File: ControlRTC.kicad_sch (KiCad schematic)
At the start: 29 parts, among them M1 Fan_4pin, SW1 SW_POWER, SW2 SW_RESET, SW3 SW_USER, SW5 SW_RECOVERY, U16 74LVC07APW, U17 LP5569RTWR, U18 PCF85063AT, Y2 X32K768S301

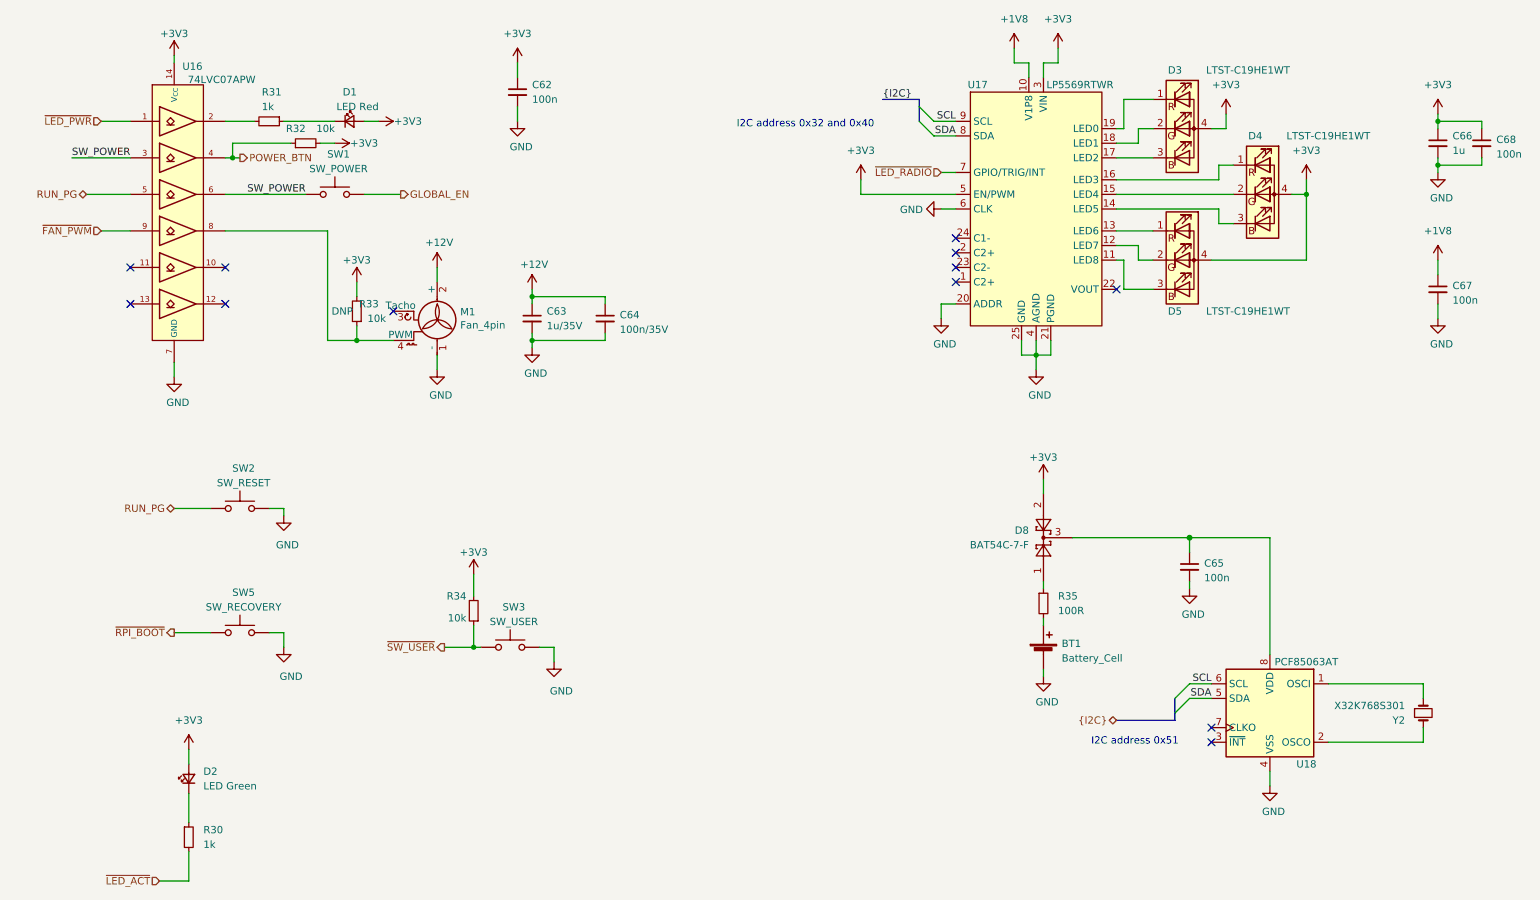
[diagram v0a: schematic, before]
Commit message: Redesign buttons/switches
Remove power/reset/recovery switch. Power and reset is not really required
and recovery mode (USB Boot) can be triggered via jumper. Make the Fan
and RPiLED a new separate config so we can leave them unpopulated. Add a
second GPIO controlled switch.

Fixes: #16

Signed-off-by: Stefan Agner <stefan@agner.ch>
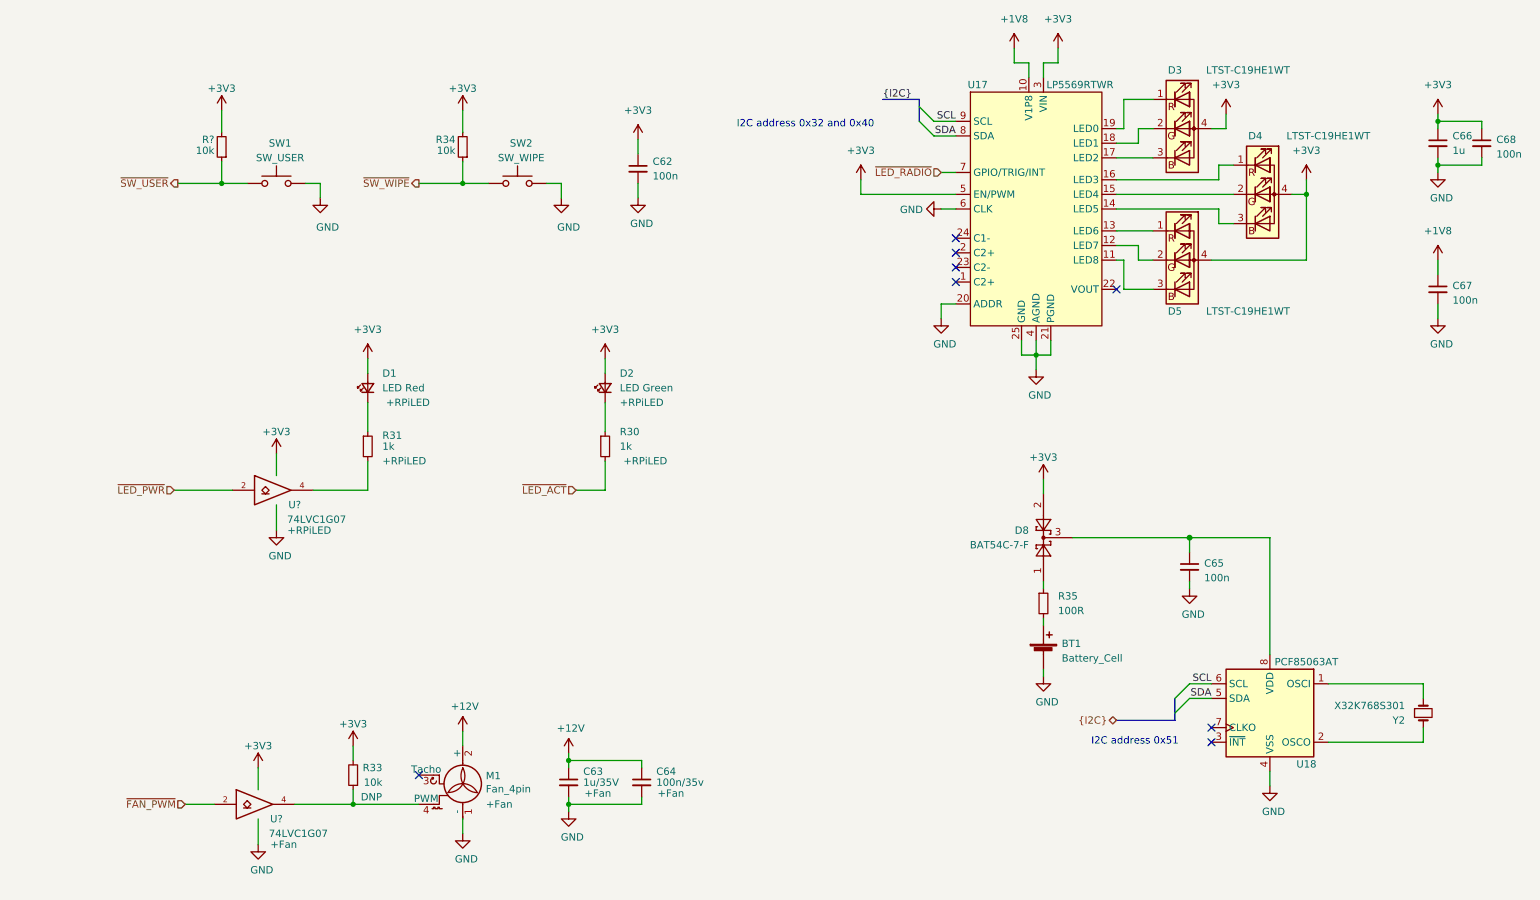
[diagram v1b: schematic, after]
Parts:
- removed R32: 10k, Resistor_SMD:R_0402_1005Metric, symbol Device:R_Small
- removed SW2: SW_RESET, Button_Switch_THT:SW_Tactile_SPST_Angled_PTS645Vx39-2LFS, symbol Switch:SW_Push
- removed SW5: SW_RECOVERY, Button_Switch_SMD:SW_SPST_B3U-3100P-B, symbol Switch:SW_Push
- removed U16: 74LVC07APW, Package_SO:TSSOP-14_4.4x5mm_P0.65mm, symbol LightBlue:74LVC07A
- added R?: 10k, Resistor_SMD:R_0402_1005Metric, symbol Device:R_Small
- added U? (x2): 74LVC1G07, symbol 74xGxx:74LVC1G07
- C63, M1: Config (none) -> +Fan
- C64: value 100n/35V -> 100n/35v; Config (none) -> +Fan
- D1, D2, R30, R31: Config (none) -> +RPiLED
- SW1: value SW_POWER -> SW_USER; footprint Button_Switch_THT:SW_Tactile_SPST_Angled_PTS645Vx39-2LFS -> Button_Switch_THT:SW_Tactile_SPST_Angled_PTS645Vx58-2LFS; PartNumber PTS645VM39-2 LFS -> PTS645VM58-2 LFS
- SW2: renamed from SW3; value SW_USER -> SW_WIPE; PartNumber PTS645VM39-2 LFS -> PTS645VK39-2 LFS
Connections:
- net GLOBAL_EN is gone; now on net GND: SW1.2
- net SW_POWER is gone; now on net ~SW_USER: SW1.1
- net +3V3: now also R?.2, U?.5 (VCC), U?.5 (VCC)
- net GND: now also U?.3 (GND), U?.3 (GND)
- net ~FAN_PWM: now also U?.2
- net ~LED_PWR: now also U?.2
- net ~SW_USER: now also R?.1; no longer R34.1, SW2.1
- net at M1.4 (PWM), R33.1: now also U?.4
- net at R31.2: now also U?.4
- new net ~SW_WIPE: R34.1, SW2.1
- no-connect marks 12 -> 8
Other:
- title: Front Panel/RTC -> Control/RTC
- moved on the sheet: C62, C63, C64, D1, D2, M1, R30, R31, R33, R34, SW2

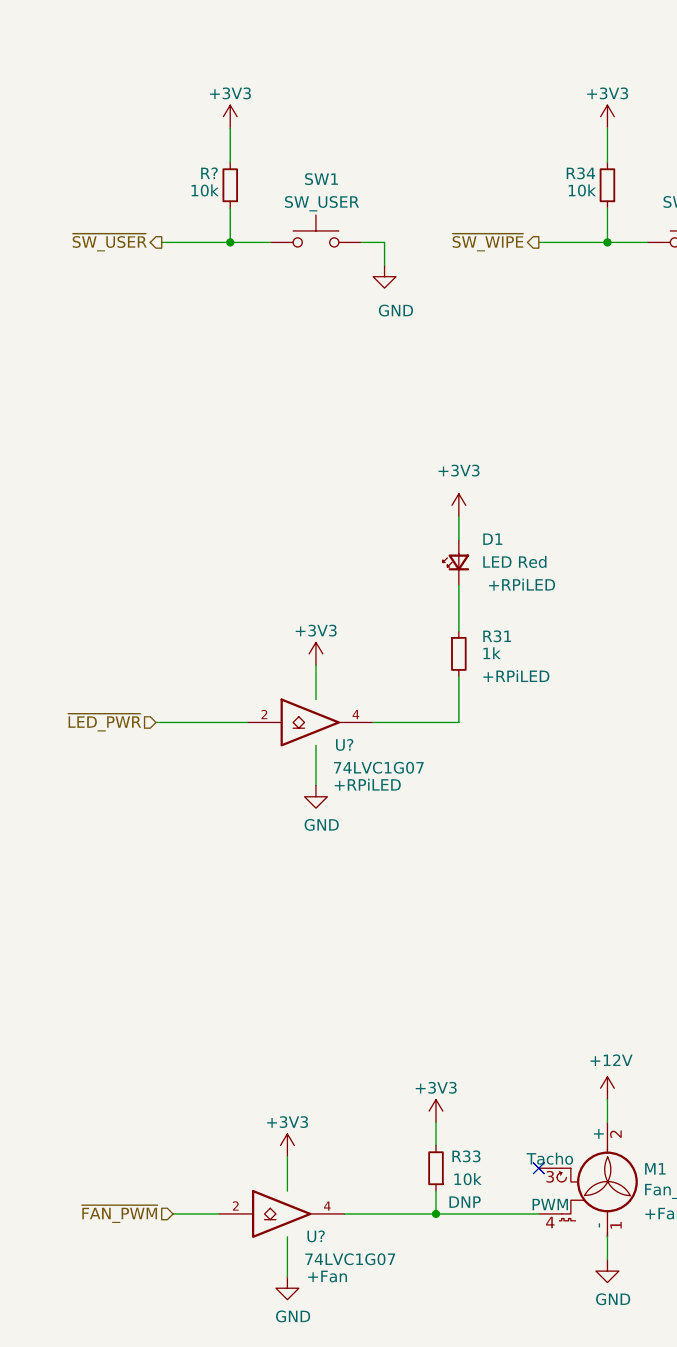
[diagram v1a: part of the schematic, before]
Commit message: Assign footprints and annotate components
Signed-off-by: Stefan Agner <stefan@agner.ch>
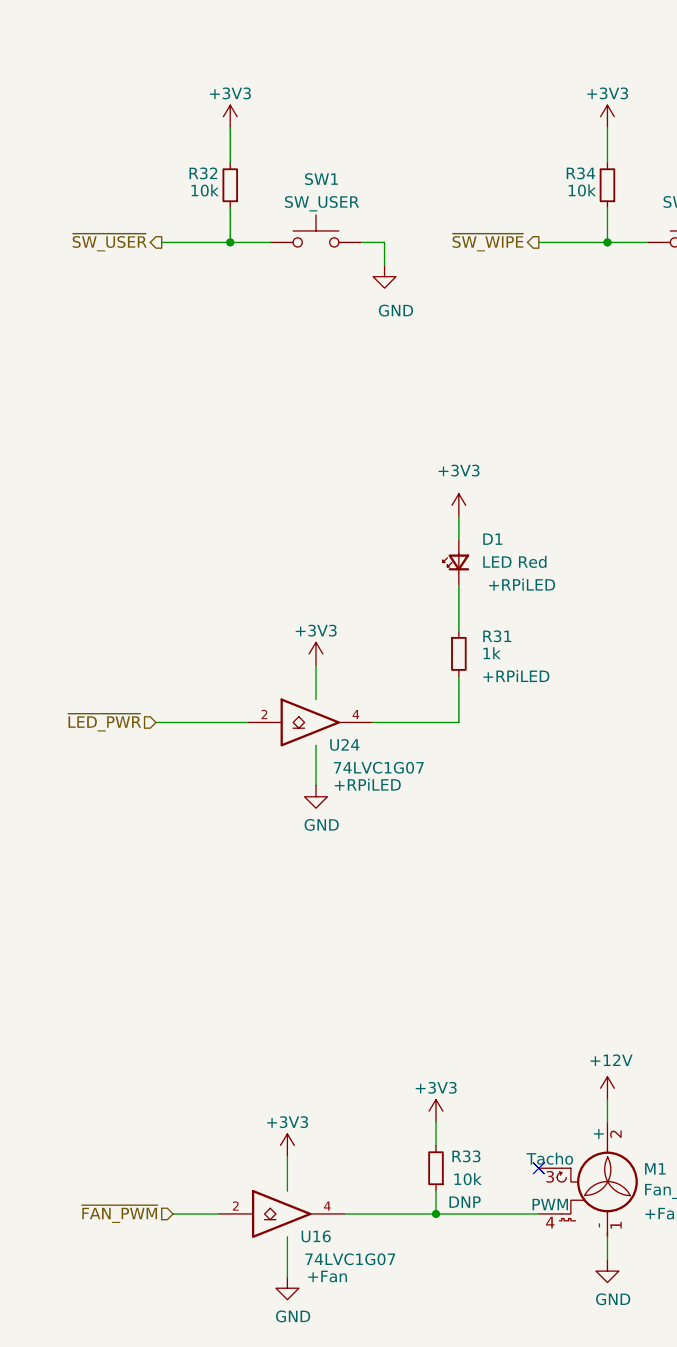
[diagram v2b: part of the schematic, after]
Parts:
- U16, U24: renamed from U?; footprint (none) -> Package_TO_SOT_SMD:SOT-353_SC-70-5
- gave numbers to parts that had none: 1
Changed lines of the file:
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@@
   (symbol (lib_id "Device:R_Small") (at 50.165 40.005 180) (unit 1)
     (in_bom yes) (on_board yes)
-    (property "Reference" "R?" (id 0) (at 48.895 38.735 0)
+    (property "Reference" "R32" (id 0) (at 48.895 38.735 0)
       (effects (font (size 1.27 1.27)) (justify left))
     )
@@
   (symbol (lib_id "74xGxx:74LVC1G07") (at 56.515 154.305 0) (unit 1)
     (in_bom yes) (on_board yes)
-    (property "Reference" "U?" (id 0) (at 59.69 156.845 0))
+    (property "Reference" "U16" (id 0) (at 59.69 156.845 0))
     (property "Value" "74LVC1G07" (id 1) (at 63.5 159.385 0))
-    (property "Footprint" "" (id 2) (at 56.515 154.305 0)
+    (property "Footprint" "Package_TO_SOT_SMD:SOT-353_SC-70-5" (id 2) (at 56.515 154.305 0)
       (effects (font (size 1.27 1.27)) hide)
     )
@@
   (symbol (lib_id "74xGxx:74LVC1G07") (at 59.69 99.695 0) (unit 1)
     (in_bom yes) (on_board yes)
-    (property "Reference" "U?" (id 0) (at 62.865 102.235 0))
+    (property "Reference" "U24" (id 0) (at 62.865 102.235 0))
     (property "Value" "74LVC1G07" (id 1) (at 66.675 104.775 0))
-    (property "Footprint" "" (id 2) (at 59.69 99.695 0)
-      (effects (font (size 1.27 1.27)) hide)
-    )
+    (property "Footprint" "Package_TO_SOT_SMD:SOT-353_SC-70-5" (id 2) (at 59.69 99.695 0)
+      (effects (font (size 1.27 1.27)) hide)
+    )

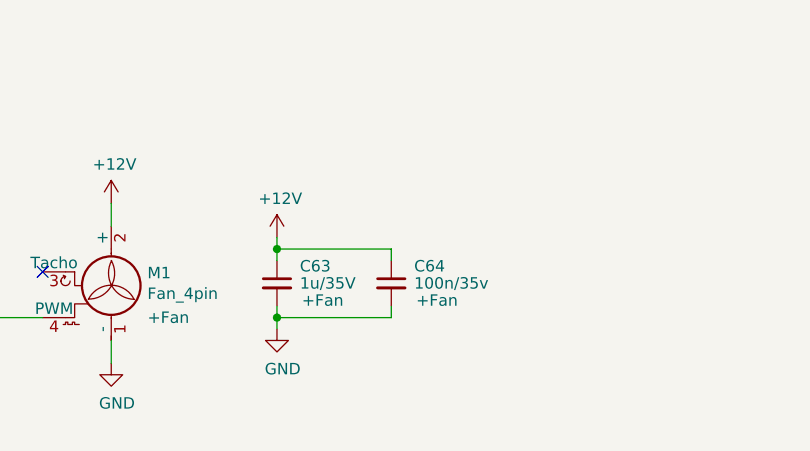
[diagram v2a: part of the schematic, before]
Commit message: Adjust various parts to improve BOM
- Replace unusual/high value ceramics with lower value in parallel
- Use the same protection Shottky Diode in PoE as in regular input
  (B340LB-13-F)
- Replace PoE rectifier Diodes with B1100-13-F
- Replace PoE Inductor (SRN6045TA-3R3Y) with the same part from 5V power
  supply (Taiyo Yuden NRS8030T3R3MJGJ)
- Correctly specify Pulse Electronics transformer

Signed-off-by: Stefan Agner <stefan@agner.ch>
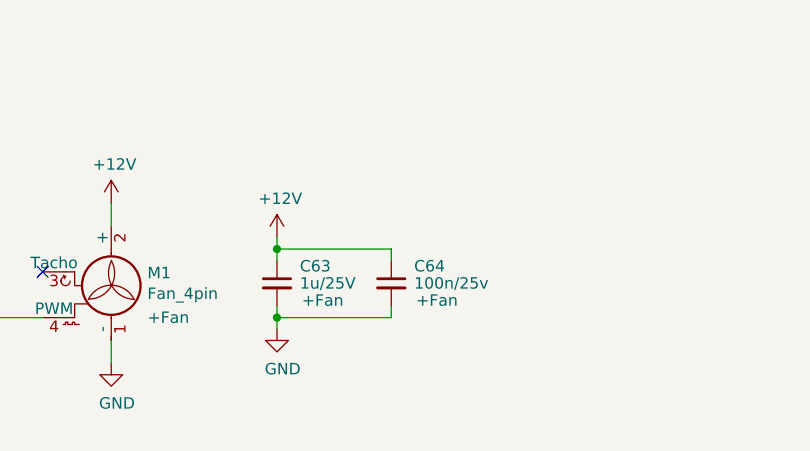
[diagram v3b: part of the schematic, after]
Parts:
- C63: value 1u/35V -> 1u/25V
- C64: value 100n/35v -> 100n/25v
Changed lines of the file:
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@@
       (effects (font (size 1.27 1.27)) (justify left))
     )
-    (property "Value" "1u/35V" (id 1) (at 113.03 150.495 0)
+    (property "Value" "1u/25V" (id 1) (at 113.03 150.495 0)
       (effects (font (size 1.27 1.27)) (justify left))
     )
@@
       (effects (font (size 1.27 1.27)) (justify left))
     )
-    (property "Value" "100n/35v" (id 1) (at 125.73 150.495 0)
+    (property "Value" "100n/25v" (id 1) (at 125.73 150.495 0)
       (effects (font (size 1.27 1.27)) (justify left))
     )

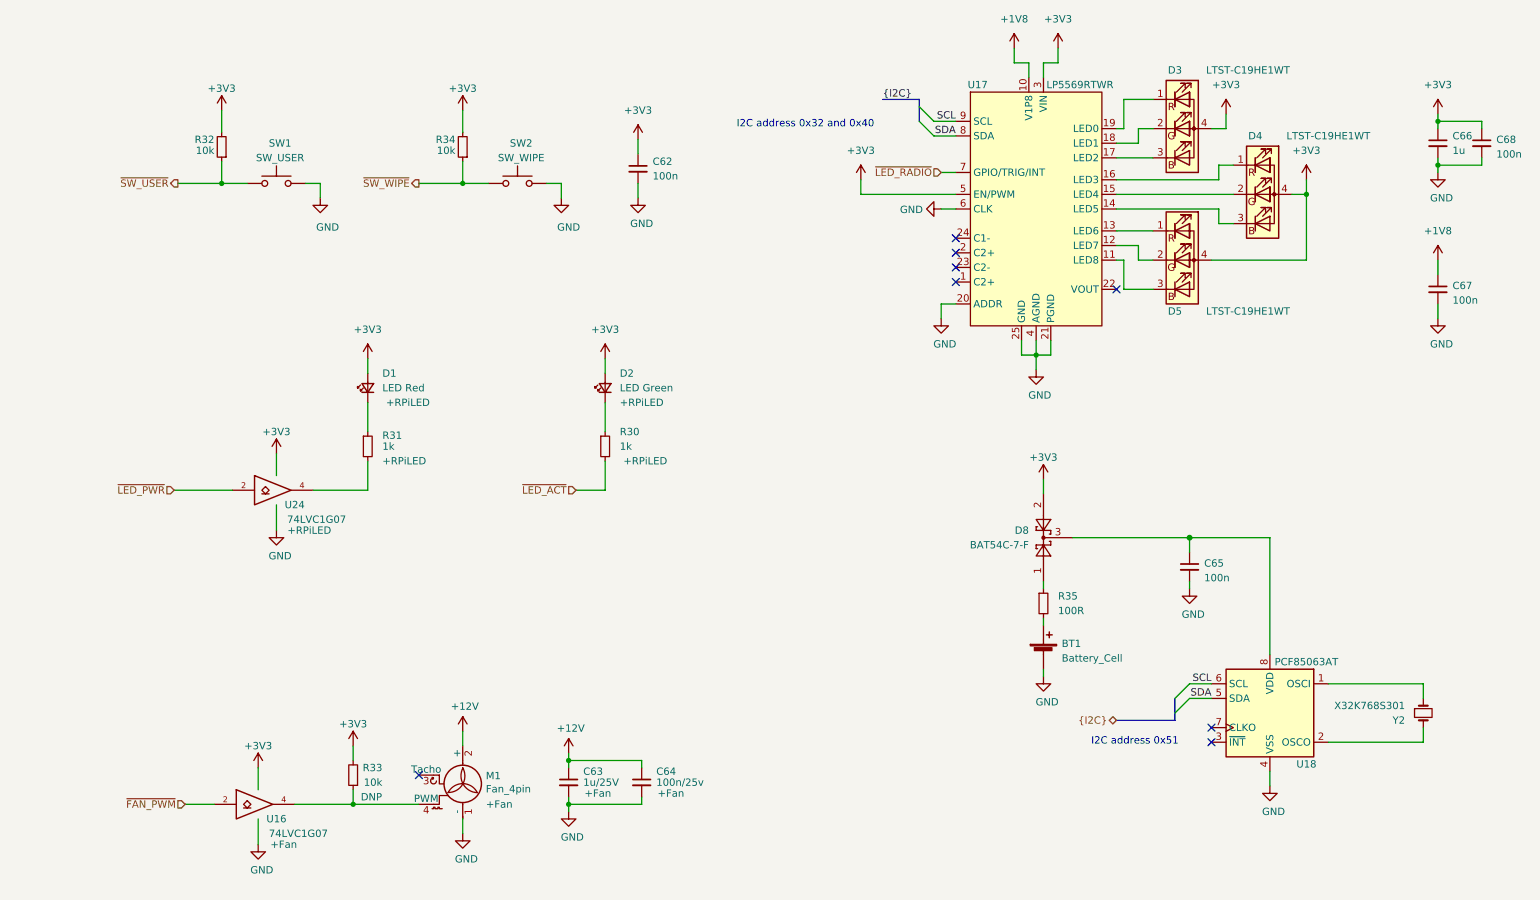
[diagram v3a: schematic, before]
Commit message: Reannotate the complete schematics
Signed-off-by: Stefan Agner <stefan@agner.ch>
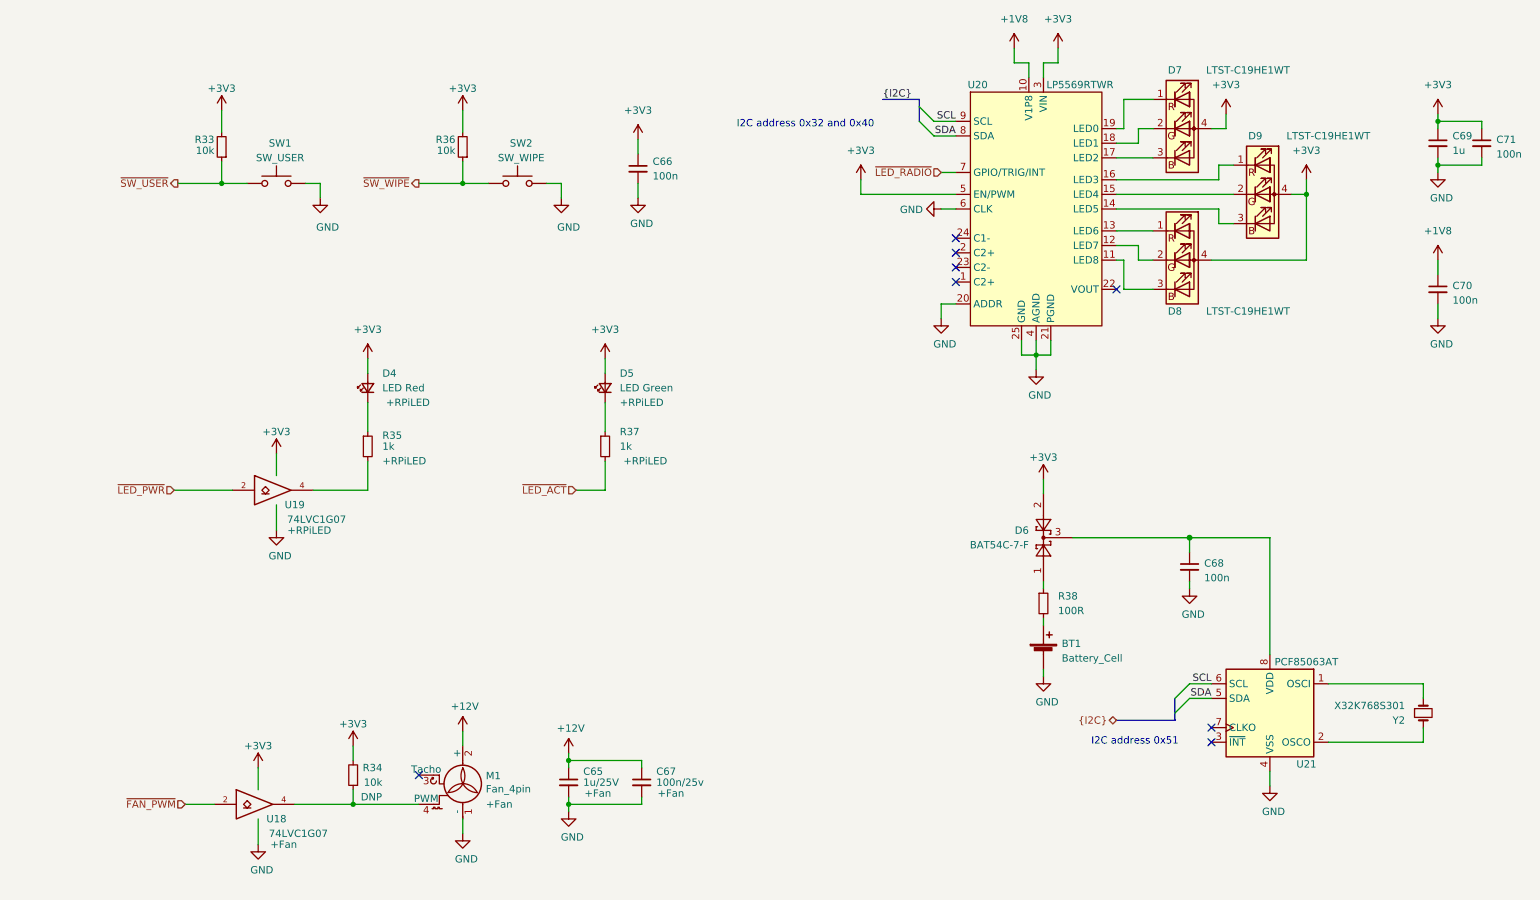
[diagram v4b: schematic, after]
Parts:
- renumbered C63 to C65, C62 to C66, C64 to C67, C65 to C68, C66 to C69, C67 to C70, C68 to C71, D1 to D4, D2 to D5, D8 to D6, D3 to D7, D5 to D8, D4 to D9, R32 to R33, R33 to R34, R31 to R35, R34 to R36, R30 to R37, R35 to R38, U16 to U18, U24 to U19, U17 to U20, U18 to U21
